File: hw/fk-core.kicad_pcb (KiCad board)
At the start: 2 copper layers, 98.8 x 37 mm, 113 parts, among them J1 RF-SMA-EDGE, J10 S2B-PH-SM4-TB, J11 RF-SMA-EDGE, J2 Conn_01x02, J4 Conn_01x01, J5 Conn_01x03, J6 Conn_01x05, J7 CONN-HDR-2x5, J9 MICRO-USB, M1 MOUNT_HOLE, M3 MOUNT_HOLE, M4 MOUNT_HOLE, M6 MOUNT_HOLE, M7 MICROSD, Q1 2N7002LT1G, Q2 2N7002LT1G, Q3 2N7002LT1G, Q4 2N7002LT1G, Q5 2N7002LT1G, SW1 SPNO, SW2 SPNO, U1 ATWINC1500-MR210PA, U10 FGPMMOPA6H, U11 MAX1704XX, U2 ATSAMD21G18A-AU, U3 RFM95W, U4 24AA02E64, U5 S25FL116K0XMFI041, U6 BQ24074RGTT, U7 PCF8523, U8 MCP1700T-3302E/MB, U9 ISL8541x, Y1 FC-135, Y2 FC-135

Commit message: Adding fiducials.
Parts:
- added M2: FIDUCIAL, RocketScreamKicadLibrary:FIDUCIAL-1MM, F.Cu at (134.7, 144.4)
- added M5: FIDUCIAL, RocketScreamKicadLibrary:FIDUCIAL-1MM, F.Cu at (174.4, 125.2)
- added M8: FIDUCIAL, RocketScreamKicadLibrary:FIDUCIAL-1MM, F.Cu at (85.8, 131.3)
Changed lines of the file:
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@@
     (tracks 1432)
     (zones 0)
-    (modules 113)
-    (nets 133)
+    (modules 116)
+    (nets 136)
   )
   (page A4)
@@
   )
   (setup
-    (last_trace_width 0.381)
+    (last_trace_width 0.254)
     (user_trace_width 0.2032)
     (user_trace_width 0.254)
@@
   (net 131 /PERIPH_GND)
   (net 132 /PERIPH_EN)
+  (net 133 "Net-(M2-Pad~)")
+  (net 134 "Net-(M5-Pad~)")
+  (net 135 "Net-(M8-Pad~)")
   (net_class Default "This is the default net class."
     (clearance 0.1524)
@@
     (add_net "Net-(J9-Pad8)")
     (add_net "Net-(J9-Pad9)")
+    (add_net "Net-(M2-Pad~)")
+    (add_net "Net-(M5-Pad~)")
     (add_net "Net-(M7-Pad1)")
     (add_net "Net-(M7-Pad8)")
     (add_net "Net-(M7-PadCD1)")
     (add_net "Net-(M7-PadCD2)")
+    (add_net "Net-(M8-Pad~)")
     (add_net "Net-(Q1-Pad3)")
     (add_net "Net-(Q2-Pad3)")
@@
       (net 1 GND))
   )
+  (module RocketScreamKicadLibrary:FIDUCIAL-1MM (layer F.Cu)
+    (at 134.7216 144.4244)
+    (descr "Circular Fiducial, 1mm bare copper top; 2.54mm keepout")
+    (tags marker)
+    (attr virtual)
+    (fp_text reference M2 (at 0 2.286) (layer F.SilkS) hide
+      (effects (font (size 1 1) (thickness 0.15)))
+    )
+    (fp_text value FIDUCIAL (at 0 -2.032) (layer F.Fab)
+      (effects (font (size 1 1) (thickness 0.15)))
+    )
+    (pad ~ smd circle (at 0 0) (size 1 1) (layers F.Cu F.Mask)
+      (net 133 "Net-(M2-Pad~)") (solder_mask_margin 0.5) (clearance 0.5))
+  )
+  (module RocketScreamKicadLibrary:FIDUCIAL-1MM (layer F.Cu)
+    (at 174.3964 125.222)
+    (descr "Circular Fiducial, 1mm bare copper top; 2.54mm keepout")
+    (tags marker)
+    (attr virtual)
+    (fp_text reference M5 (at 0 2.286) (layer F.SilkS) hide
+      (effects (font (size 1 1) (thickness 0.15)))
+    )
+    (fp_text value FIDUCIAL (at 0 -2.032) (layer F.Fab)
+      (effects (font (size 1 1) (thickness 0.15)))
+    )
+    (pad ~ smd circle (at 0 0) (size 1 1) (layers F.Cu F.Mask)
+      (net 134 "Net-(M5-Pad~)") (solder_mask_margin 0.5) (clearance 0.5))
+  )
+  (module RocketScreamKicadLibrary:FIDUCIAL-1MM (layer F.Cu)
+    (at 85.7504 131.318)
+    (descr "Circular Fiducial, 1mm bare copper top; 2.54mm keepout")
+    (tags marker)
+    (attr virtual)
+    (fp_text reference M8 (at 0 2.286) (layer F.SilkS) hide
+      (effects (font (size 1 1) (thickness 0.15)))
+    )
+    (fp_text value FIDUCIAL (at 0 -2.032) (layer F.Fab)
+      (effects (font (size 1 1) (thickness 0.15)))
+    )
+    (pad ~ smd circle (at 0 0) (size 1 1) (layers F.Cu F.Mask)
+      (net 135 "Net-(M8-Pad~)") (solder_mask_margin 0.5) (clearance 0.5))
+  )
   (gr_circle (center 101.4984 123.5964) (end 101.4484 123.5464) (layer F.SilkS) (width 0.3))

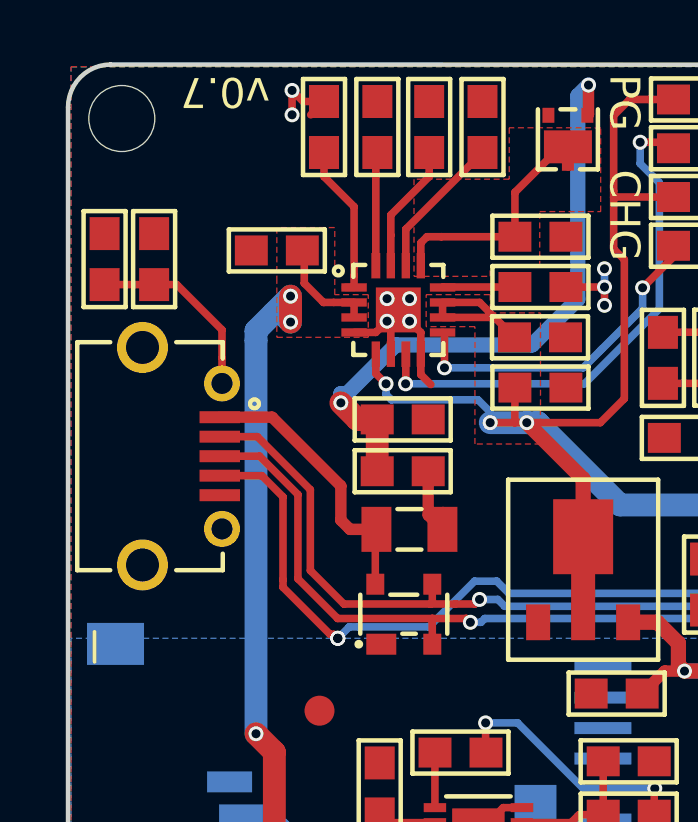
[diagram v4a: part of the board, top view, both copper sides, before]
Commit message: Separate USB and SD a little more.
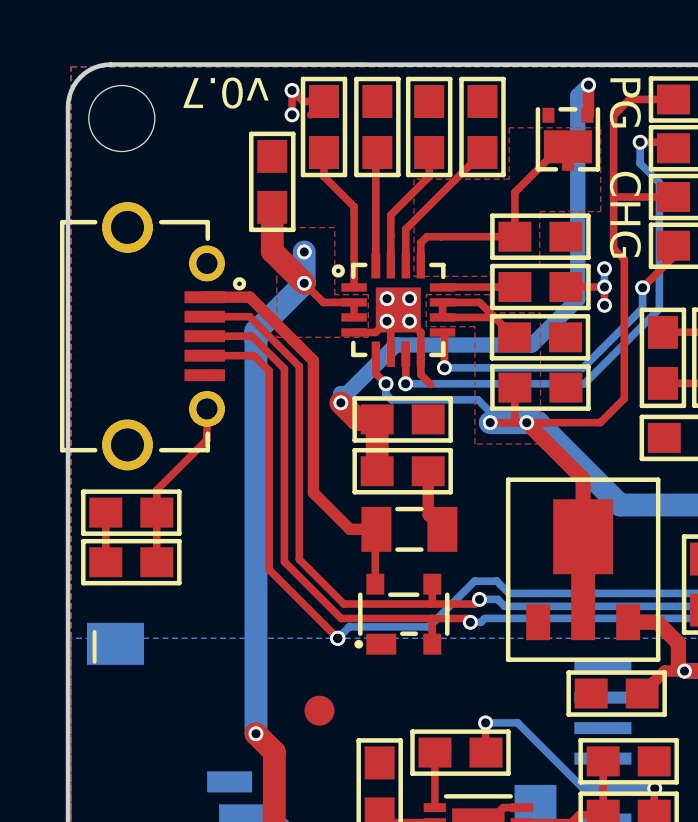
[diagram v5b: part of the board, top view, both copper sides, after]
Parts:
- moved R31 10.1 mm to (79.5, 126.4), turned to 180 degrees
- moved C14 8.49 mm to (79.5, 124.7), turned to 180 degrees
- moved J9 4.03 mm to (80.5, 118.8)
- moved C19 2.29 mm to (84.2, 113.7), turned to 90 degrees
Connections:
- J9 pad 6: Net-(C14-Pad1) -> Net-(J9-Pad6)
- J9 pad 7: Net-(J9-Pad7) -> Net-(C14-Pad1)
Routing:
- net /USB-: track 57.0 -> 61.4 mm
- net /USB+: track 54.8 -> 59.1 mm
- net Net-(J9-Pad4): track 58.8 -> 63.1 mm
- net VUSB: track 9.28 -> 13.4 mm
- net VBAT: track 45.3 -> 47.9 mm
- net GND: track 80.1 -> 81.7 mm
- net Net-(C14-Pad1): track 6.32 -> 5.80 mm
